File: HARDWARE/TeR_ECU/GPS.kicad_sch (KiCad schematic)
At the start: 3 parts, among them J6 Conn_Coaxial, U8 NEO-M9N

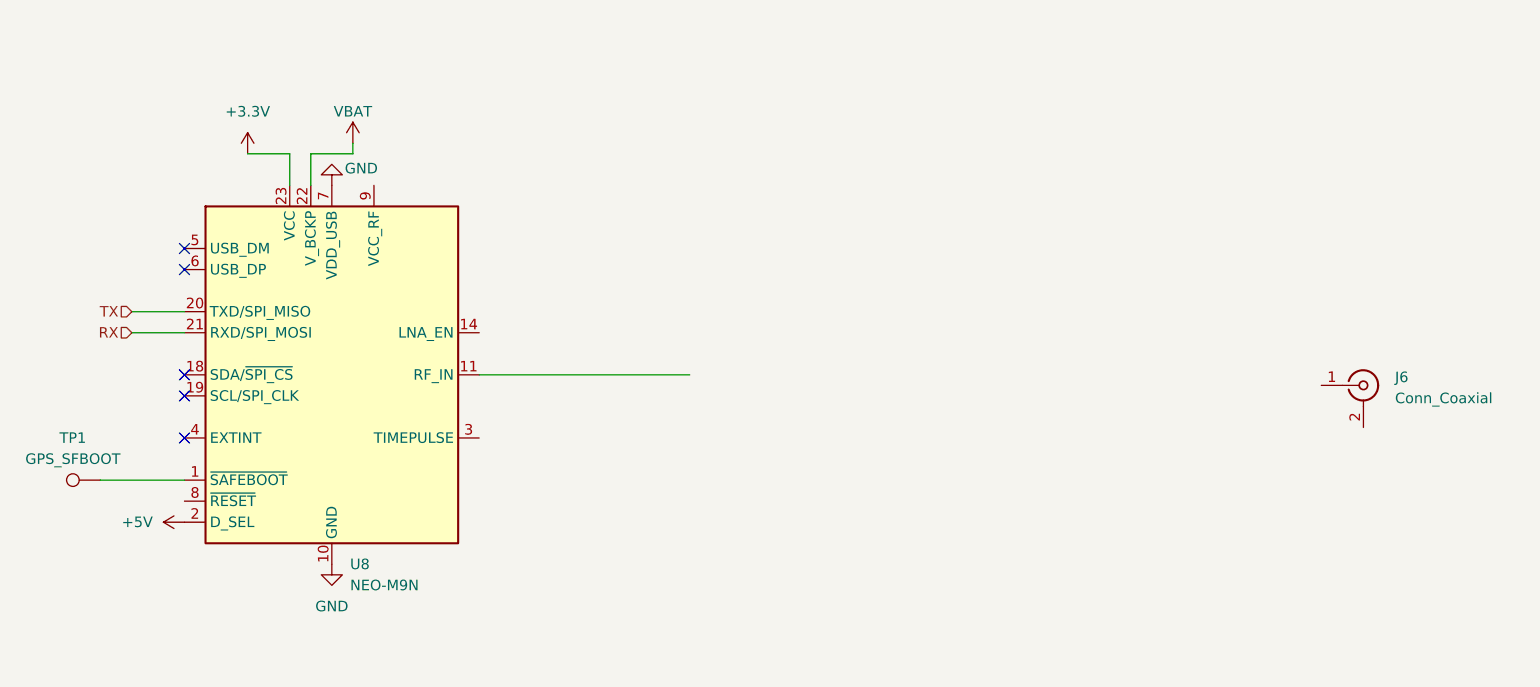
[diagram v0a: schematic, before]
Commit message: Advanced RF fronted BIAS-T for LNA antenna and digital input redesign
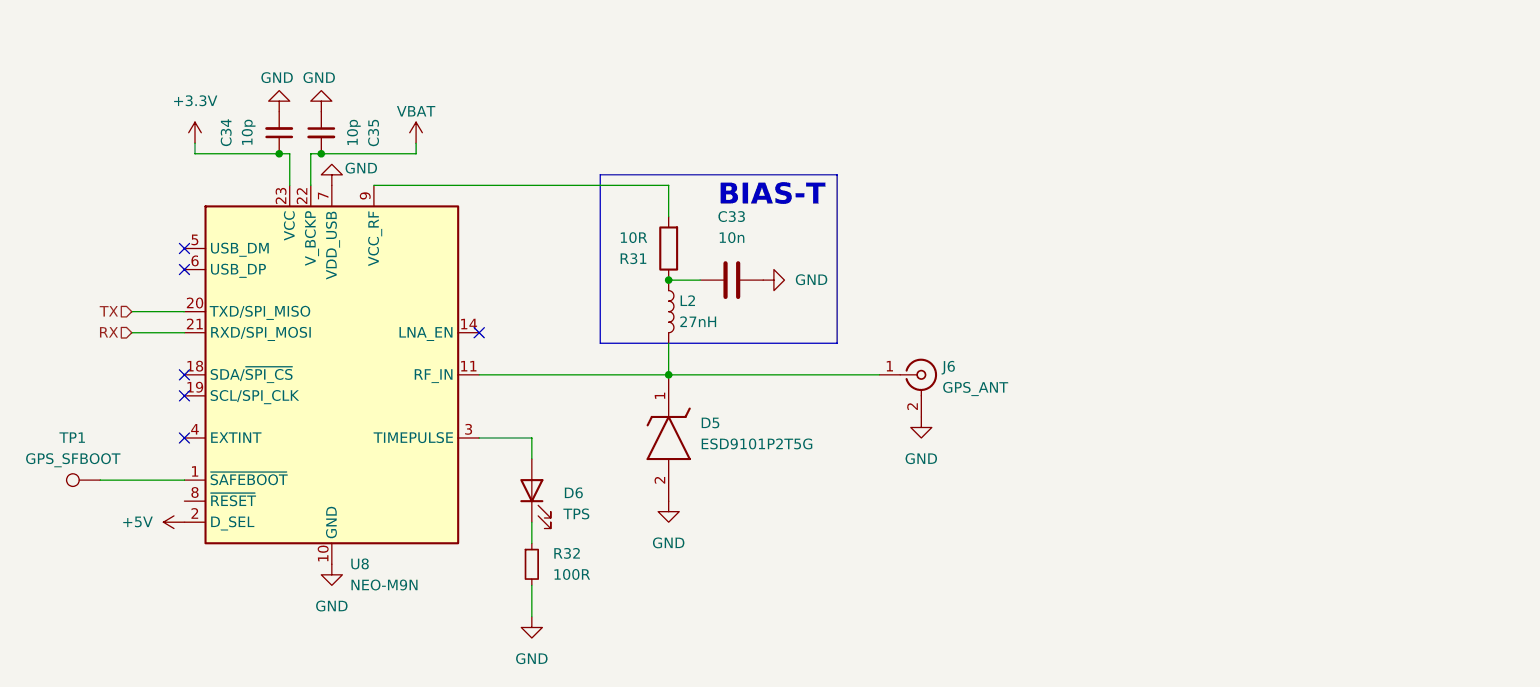
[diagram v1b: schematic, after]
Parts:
- added C33: 10n, symbol Device:C
- added C34, C35: 10p, symbol Device:C_Small
- added D5: ESD9101P2T5G, SODFL1006X40N, symbol DIODO_GPS:ESD9101P2T5G
- added D6: TPS, symbol Device:LED
- added L2: 27nH, symbol Device:L
- added R31: 10R, symbol Device:R
- added R32: 100R, symbol Device:R_Small
- J6: value Conn_Coaxial -> GPS_ANT
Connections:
- net +3.3V: now also C34.1
- net GND: now also J6.2 (Ext), C33.2, C34.2, C35.1, D5.2 (A), R32.2
- net VBAT: now also C35.2
- net at J6.1 (In): now also U8.11 (RF_IN), D5.1 (K), L2.2
- net at U8.3 (TIMEPULSE): now also D6.2 (A)
- net at U8.9 (VCC_RF): now also R31.2
- new net: C33.1, L2.1, R31.1
- new net: D6.1 (K), R32.1
- no-connect marks 5 -> 6
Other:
- note added: "BIAS-T"
- moved on the sheet: J6

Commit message: Quick changes, go to start layouting
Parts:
- C40: renamed from C34; footprint (none) -> Capacitor_SMD:C_0603_1608Metric
- C41: renamed from C35; footprint (none) -> Capacitor_SMD:C_0603_1608Metric
- C42: renamed from C33; footprint (none) -> Capacitor_SMD:C_0603_1608Metric
- D25: renamed from D6; footprint (none) -> LED_SMD:LED_0201_0603Metric
- renumbered D5 to D26, J6 to J5, R32 to R45, R31 to R46, U8 to U10
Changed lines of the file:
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@@
 		(dnp no)
 		(fields_autoplaced yes)
-		(property "Reference" "#PWR091"
+		(property "Reference" "#PWR0119"
 			(at 106.68 110.49 0)
 			(effects
@@
 			(project "TeR_ECU"
 				(path "/84413845-c4f3-4743-bcd2-a67649c90902/7ff49dfd-e79b-4d4a-bad4-beb43905c8a0"
-					(reference "#PWR091")
+					(reference "#PWR0119")
 					(unit 1)
 				)
@@
 		(on_board yes)
 		(dnp no)
-		(property "Reference" "#PWR090"
+		(property "Reference" "#PWR0123"
 			(at 120.65 63.5 0)
 			(effects
@@
 			(project "TeR_ECU"
 				(path "/84413845-c4f3-4743-bcd2-a67649c90902/7ff49dfd-e79b-4d4a-bad4-beb43905c8a0"
-					(reference "#PWR090")
+					(reference "#PWR0123")
 					(unit 1)
 				)
@@
 		(dnp no)
 		(fields_autoplaced yes)
-		(property "Reference" "D5"
+		(property "Reference" "D26"
 			(at 165.1 98.5519 90)
 			(effects
@@
 			(project ""
 				(path "/84413845-c4f3-4743-bcd2-a67649c90902/7ff49dfd-e79b-4d4a-bad4-beb43905c8a0"
-					(reference "D5")
+					(reference "D26")
 					(unit 1)
 				)
@@
 		(on_board yes)
 		(dnp no)
-		(property "Reference" "#PWR097"
+		(property "Reference" "#PWR0122"
 			(at 119.38 54.61 0)
 			(effects
@@
 			(project "TeR_ECU"
 				(path "/84413845-c4f3-4743-bcd2-a67649c90902/7ff49dfd-e79b-4d4a-bad4-beb43905c8a0"
-					(reference "#PWR097")
+					(reference "#PWR0122")
 					(unit 1)
 				)
@@
 		(dnp no)
 		(fields_autoplaced yes)
-		(property "Reference" "#PWR094"
+		(property "Reference" "#PWR0128"
 			(at 179.07 81.28 0)
 			(effects
@@
 			(project "TeR_ECU"
 				(path "/84413845-c4f3-4743-bcd2-a67649c90902/7ff49dfd-e79b-4d4a-bad4-beb43905c8a0"
-					(reference "#PWR094")
+					(reference "#PWR0128")
 					(unit 1)
 				)
@@
 		(dnp no)
 		(fields_autoplaced yes)
-		(property "Reference" "#PWR095"
+		(property "Reference" "#PWR0127"
 			(at 161.29 114.3 0)
 			(effects
@@
 			(project "TeR_ECU"
 				(path "/84413845-c4f3-4743-bcd2-a67649c90902/7ff49dfd-e79b-4d4a-bad4-beb43905c8a0"
-					(reference "#PWR095")
+					(reference "#PWR0127")
 					(unit 1)
 				)
@@
 		(dnp no)
 		(fields_autoplaced yes)
-		(property "Reference" "#PWR093"
+		(property "Reference" "#PWR0129"
 			(at 191.77 104.14 0)
 			(effects
@@
 			(project ""
 				(path "/84413845-c4f3-4743-bcd2-a67649c90902/7ff49dfd-e79b-4d4a-bad4-beb43905c8a0"
-					(reference "#PWR093")
+					(reference "#PWR0129")
 					(unit 1)
 				)
@@
 		(on_board yes)
 		(dnp no)
-		(property "Reference" "#PWR096"
+		(property "Reference" "#PWR0121"
 			(at 114.3 54.61 0)
 			(effects
@@
 			(project "TeR_ECU"
 				(path "/84413845-c4f3-4743-bcd2-a67649c90902/7ff49dfd-e79b-4d4a-bad4-beb43905c8a0"
-					(reference "#PWR096")
+					(reference "#PWR0121")
 					(unit 1)
 				)
@@
 		(dnp no)
 		(fields_autoplaced yes)
-		(property "Reference" "R32"
+		(property "Reference" "R45"
 			(at 147.32 114.2999 0)
 			(effects
@@
 			(project ""
 				(path "/84413845-c4f3-4743-bcd2-a67649c90902/7ff49dfd-e79b-4d4a-bad4-beb43905c8a0"
-					(reference "R32")
+					(reference "R45")
 					(unit 1)
 				)
@@
 		(dnp no)
 		(fields_autoplaced yes)
-		(property "Reference" "J6"
+		(property "Reference" "J5"
 			(at 194.31 91.7331 0)
 			(effects
@@
 			(project ""
 				(path "/84413845-c4f3-4743-bcd2-a67649c90902/7ff49dfd-e79b-4d4a-bad4-beb43905c8a0"
-					(reference "J6")
+					(reference "J5")
 					(unit 1)
 				)
@@
 		(dnp no)
 		(fields_autoplaced yes)
-		(property "Reference" "#PWR092"
+		(property "Reference" "#PWR0124"
 			(at 120.65 121.92 0)
 			(effects
@@
 			(project "TeR_ECU"
 				(path "/84413845-c4f3-4743-bcd2-a67649c90902/7ff49dfd-e79b-4d4a-bad4-beb43905c8a0"
-					(reference "#PWR092")
+					(reference "#PWR0124")
 					(unit 1)
 				)
@@
 		(on_board yes)
 		(dnp no)
-		(property "Reference" "#PWR088"
+		(property "Reference" "#PWR0125"
 			(at 130.81 68.58 0)
 			(effects
@@
 			(project "TeR_ECU"
 				(path "/84413845-c4f3-4743-bcd2-a67649c90902/7ff49dfd-e79b-4d4a-bad4-beb43905c8a0"
-					(reference "#PWR088")
+					(reference "#PWR0125")
 					(unit 1)
 				)
@@
 		(on_board yes)
 		(dnp no)
-		(property "Reference" "C35"
+		(property "Reference" "C41"
 			(at 125.73 63.5064 90)
 			(effects
@@
 			)
 		)
-		(property "Footprint" ""
+		(property "Footprint" "Capacitor_SMD:C_0603_1608Metric"
 			(at 119.38 63.5 0)
 			(effects
@@
 			(project "TeR_ECU"
 				(path "/84413845-c4f3-4743-bcd2-a67649c90902/7ff49dfd-e79b-4d4a-bad4-beb43905c8a0"
-					(reference "C35")
+					(reference "C41")
 					(unit 1)
 				)
@@
 		(dnp no)
 		(fields_autoplaced yes)
-		(property "Reference" "D6"
+		(property "Reference" "D25"
 			(at 148.59 106.9974 90)
 			(effects
@@
 			)
 		)
-		(property "Footprint" ""
+		(property "Footprint" "LED_SMD:LED_0201_0603Metric"
 			(at 144.78 106.68 0)
 			(effects
@@
 			(project ""
 				(path "/84413845-c4f3-4743-bcd2-a67649c90902/7ff49dfd-e79b-4d4a-bad4-beb43905c8a0"
-					(reference "D6")
+					(reference "D25")
 					(unit 1)
 				)
@@
 		(on_board yes)
 		(dnp no)
-		(property "Reference" "R31"
+		(property "Reference" "R46"
 			(at 158.75 78.7401 0)
 			(effects
@@
 			(project ""
 				(path "/84413845-c4f3-4743-bcd2-a67649c90902/7ff49dfd-e79b-4d4a-bad4-beb43905c8a0"
-					(reference "R31")
+					(reference "R46")
 					(unit 1)
 				)
@@
 		(dnp no)
 		(fields_autoplaced yes)
-		(property "Reference" "C33"
+		(property "Reference" "C42"
 			(at 168.91 73.66 90)
 			(effects
@@
 			)
 		)
-		(property "Footprint" ""
+		(property "Footprint" "Capacitor_SMD:C_0603_1608Metric"
 			(at 172.72 80.3148 0)
 			(effects
@@
 			(project ""
 				(path "/84413845-c4f3-4743-bcd2-a67649c90902/7ff49dfd-e79b-4d4a-bad4-beb43905c8a0"
-					(reference "C33")
+					(reference "C42")
 					(unit 1)
 				)
@@
 		(dnp no)
 		(fields_autoplaced yes)
-		(property "Reference" "#PWR098"
+		(property "Reference" "#PWR0126"
 			(at 144.78 128.27 0)
 			(effects
@@
 			(project ""
 				(path "/84413845-c4f3-4743-bcd2-a67649c90902/7ff49dfd-e79b-4d4a-bad4-beb43905c8a0"
-					(reference "#PWR098")
+					(reference "#PWR0126")
 					(unit 1)
 				)
@@
 		(dnp no)
 		(fields_autoplaced yes)
-		(property "Reference" "#PWR089"
+		(property "Reference" "#PWR0120"
 			(at 104.14 68.58 0)
 			(effects
@@
 			(project "TeR_ECU"
 				(path "/84413845-c4f3-4743-bcd2-a67649c90902/7ff49dfd-e79b-4d4a-bad4-beb43905c8a0"
-					(reference "#PWR089")
+					(reference "#PWR0120")
 					(unit 1)
 				)
@@
 		(on_board yes)
 		(dnp no)
-		(property "Reference" "C34"
+		(property "Reference" "C40"
 			(at 107.95 63.4936 90)
 			(effects
@@
 			)
 		)
-		(property "Footprint" ""
+		(property "Footprint" "Capacitor_SMD:C_0603_1608Metric"
 			(at 114.3 63.5 0)
 			(effects
@@
 			(project "TeR_ECU"
 				(path "/84413845-c4f3-4743-bcd2-a67649c90902/7ff49dfd-e79b-4d4a-bad4-beb43905c8a0"
-					(reference "C34")
+					(reference "C40")
 					(unit 1)
 				)
@@
 		(dnp no)
 		(fields_autoplaced yes)
-		(property "Reference" "U8"
+		(property "Reference" "U10"
 			(at 122.8441 115.57 0)
 			(effects
@@
 			(project "TeR_ECU"
 				(path "/84413845-c4f3-4743-bcd2-a67649c90902/7ff49dfd-e79b-4d4a-bad4-beb43905c8a0"
-					(reference "U8")
-					(unit 1)
-				)
+					(reference "U10")
+					(unit 1)
+				)

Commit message: Began layout
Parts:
- J5: footprint (none) -> Connector_Coaxial:SMA_Amphenol_132289_EdgeMount
- L2: footprint (none) -> Inductor_SMD:L_0805_2012Metric
- R45, R46: footprint (none) -> Resistor_SMD:R_0603_1608Metric
- TP1: footprint (none) -> TestPoint:TestPoint_Pad_1.0x1.0mm
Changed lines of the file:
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@@
 			)
 		)
-		(property "Footprint" ""
+		(property "Footprint" "Inductor_SMD:L_0805_2012Metric"
 			(at 161.29 85.09 0)
 			(effects
@@
 			)
 		)
-		(property "Footprint" ""
+		(property "Footprint" "Resistor_SMD:R_0603_1608Metric"
 			(at 144.78 115.57 0)
 			(effects
@@
 			)
 		)
-		(property "Footprint" ""
+		(property "Footprint" "Connector_Coaxial:SMA_Amphenol_132289_EdgeMount"
 			(at 191.77 92.71 0)
 			(effects
@@
 			)
 		)
-		(property "Footprint" ""
+		(property "Footprint" "Resistor_SMD:R_0603_1608Metric"
 			(at 163.068 77.47 90)
 			(effects
@@
 			)
 		)
-		(property "Footprint" ""
+		(property "Footprint" "TestPoint:TestPoint_Pad_1.0x1.0mm"
 			(at 92.71 100.33 0)
 			(effects

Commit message: First layout prototype
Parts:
- D25: footprint LED_SMD:LED_0201_0603Metric -> LED_SMD:LED_0603_1608Metric
- D26: footprint SODFL1006X40N -> GPS_D:SODFL1006X40N
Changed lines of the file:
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@@
 			)
 		)
-		(property "Footprint" "SODFL1006X40N"
+		(property "Footprint" "GPS_D:SODFL1006X40N"
 			(at 67.64 102.87 0)
 			(effects
@@
 			)
 		)
-		(property "Footprint" "LED_SMD:LED_0201_0603Metric"
+		(property "Footprint" "LED_SMD:LED_0603_1608Metric"
 			(at 144.78 106.68 0)
 			(effects

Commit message: Finished layout, RF design, and quick DRC check, Lookin gud
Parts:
- removed C41: 10p, Capacitor_SMD:C_0603_1608Metric, symbol Device:C_Small
- added JP3: EN_USB, Jumper:SolderJumper-2_P1.3mm_Open_RoundedPad1.0x1.5mm, symbol Jumper:SolderJumper_2_Open
- added R41: 100k, Resistor_SMD:R_0603_1608Metric, symbol Device:R_Small
- added R44, R53: 27R, Resistor_SMD:R_0603_1608Metric, symbol Device:R_Small
- added TP2: USB+, TestPoint:TestPoint_Pad_1.0x1.0mm, symbol Connector:TestPoint
- added TP3: USB-, TestPoint:TestPoint_Pad_1.0x1.0mm, symbol Connector:TestPoint
- C42: footprint Capacitor_SMD:C_0603_1608Metric -> Capacitor_SMD:C_0402_1005Metric
- L2: footprint Inductor_SMD:L_0805_2012Metric -> Inductor_SMD:L_0402_1005Metric
- R46: footprint Resistor_SMD:R_0603_1608Metric -> Resistor_SMD:R_0402_1005Metric
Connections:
- net +5V is gone; now on net +3.3V: U10.2 (D_SEL)
- net VBAT is gone; now on net +3.3V: U10.22 (V_BCKP)
- net +3.3V: now also JP3.2 (B)
- net GND: now also R41.2; no longer U10.7 (VDD_USB)
- net at U10.5 (USB_DM): now also R44.2
- net at U10.6 (USB_DP): now also R53.1
- new net: R53.2, TP2.1
- new net: R44.1, TP3.1
- new net: JP3.1 (A), R41.1, U10.7 (VDD_USB)
- no-connect marks 6 -> 5
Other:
- moved on the sheet: C40, TP1
